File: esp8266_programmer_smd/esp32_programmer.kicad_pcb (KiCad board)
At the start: 2 copper layers, 39.2 x 54 mm, 42 parts, among them P1 USB_C_Plug_USB2.0, Q1 S8050, Q2 S8050, SW1 SW_Push, SW2 SW_Push, U1 CH340C, U2 ESP-12E

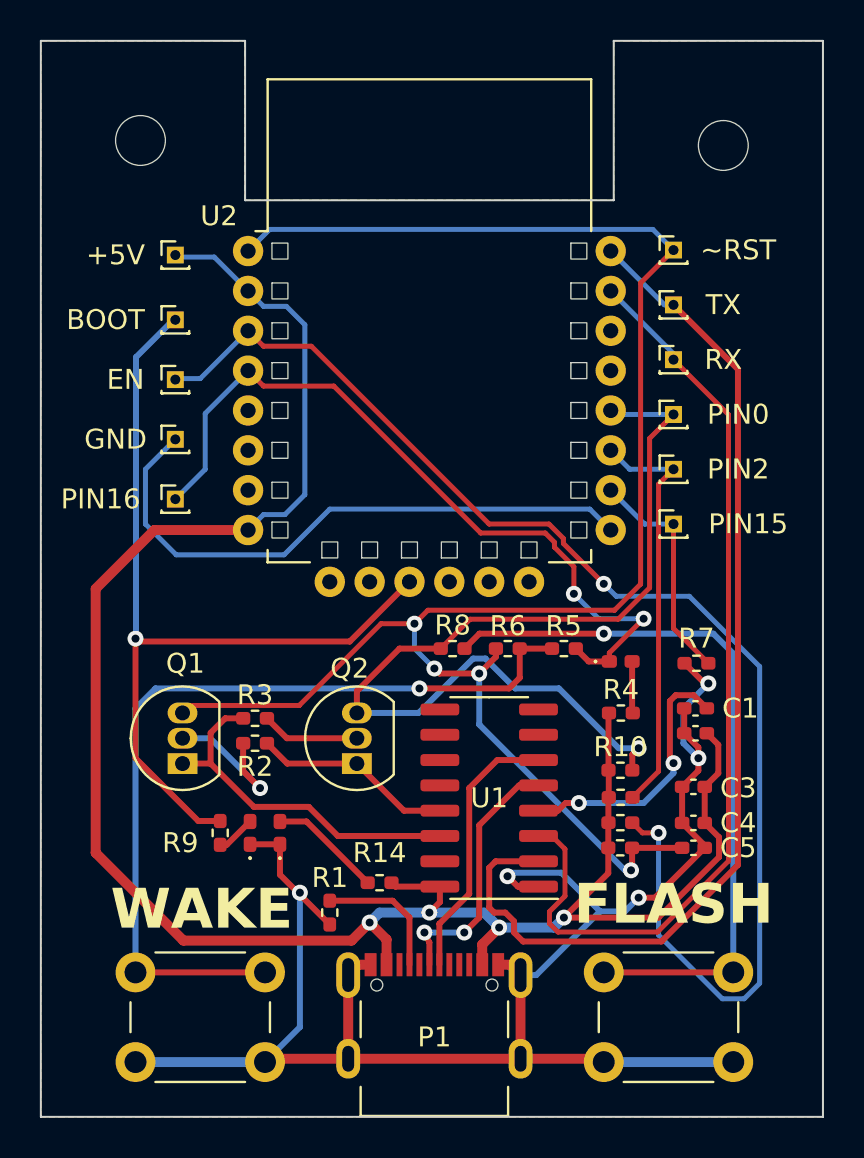
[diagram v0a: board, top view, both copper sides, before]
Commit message: Updated #6 pcb problem
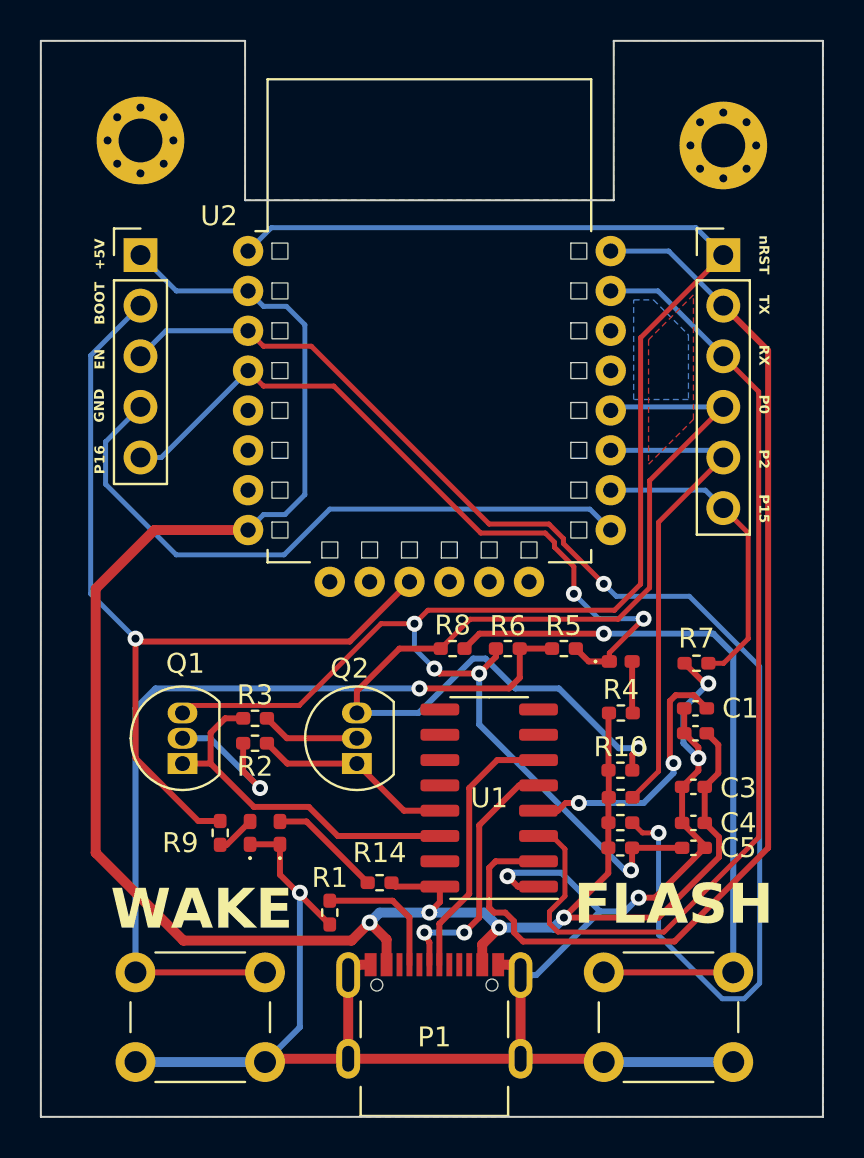
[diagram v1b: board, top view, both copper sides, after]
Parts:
- removed +5V, BOOT, EN, GND, PIN0, PIN15, PIN16, PIN2, RX, TX, ~RST: MountingHole_Pad, Connector_PinHeader_1.00mm:PinHeader_1x01_P1.00mm_Vertical
- added G***: LOGO, Graphics:GithubQR, B.Cu at (145.5, 99.8)
- added J1: Conn_01x05_Pin, Connector_PinHeader_2.54mm:PinHeader_1x05_P2.54mm_Vertical, F.Cu at (131.0, 93.8)
- added J2: Conn_01x06_Pin, Connector_PinHeader_2.54mm:PinHeader_1x06_P2.54mm_Vertical, F.Cu at (160.2, 93.8)
- H12, H13: value MountingHole -> MountingHole_Pad; footprint MountingHole:MountingHole_2.5mm -> MountingHole:MountingHole_2.2mm_M2_Pad_Via
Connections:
- net /BOOT_LED renamed BOOT_LED
- net /EN renamed EN
- net /PIN0 renamed PIN0
- net /PIN15 renamed PIN15
- net /PIN16 renamed PIN16
- net /PIN2 renamed PIN2
- net /RX renamed RX
- net /TX renamed TX
- net /nRST renamed nRST
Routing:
- net PIN0: track 48.7 -> 52.9 mm
- net PIN15: track 11.6 -> 15.6 mm
- net PIN2: track 20.9 -> 24.7 mm
- net nRST: track 89.0 -> 92.5 mm
- net TX: track 53.4 -> 56.5 mm
- net RX: track 47.4 -> 50.2 mm
- net GND: track 121.3 -> 123.9 mm
- net VBUS: track 104.6 -> 106.4 mm
- net BOOT_LED: track 43.5 -> 45.3 mm
- net EN: track 66.8 -> 68.1 mm
- net PIN16: track 39.0 -> 38.2 mm
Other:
- board text added: "+5V"
- board text added: "BOOT"
- board text added: "EN"
- board text added: "GND"
- board text added: "P0"
- board text added: "P15"
- board text added: "P16"
- board text added: "P2"
- board text added: "RX"
- board text added: "TX"
- board text added: "nRST"
